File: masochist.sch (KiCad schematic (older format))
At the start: 76 parts, among them Y1 Crystal

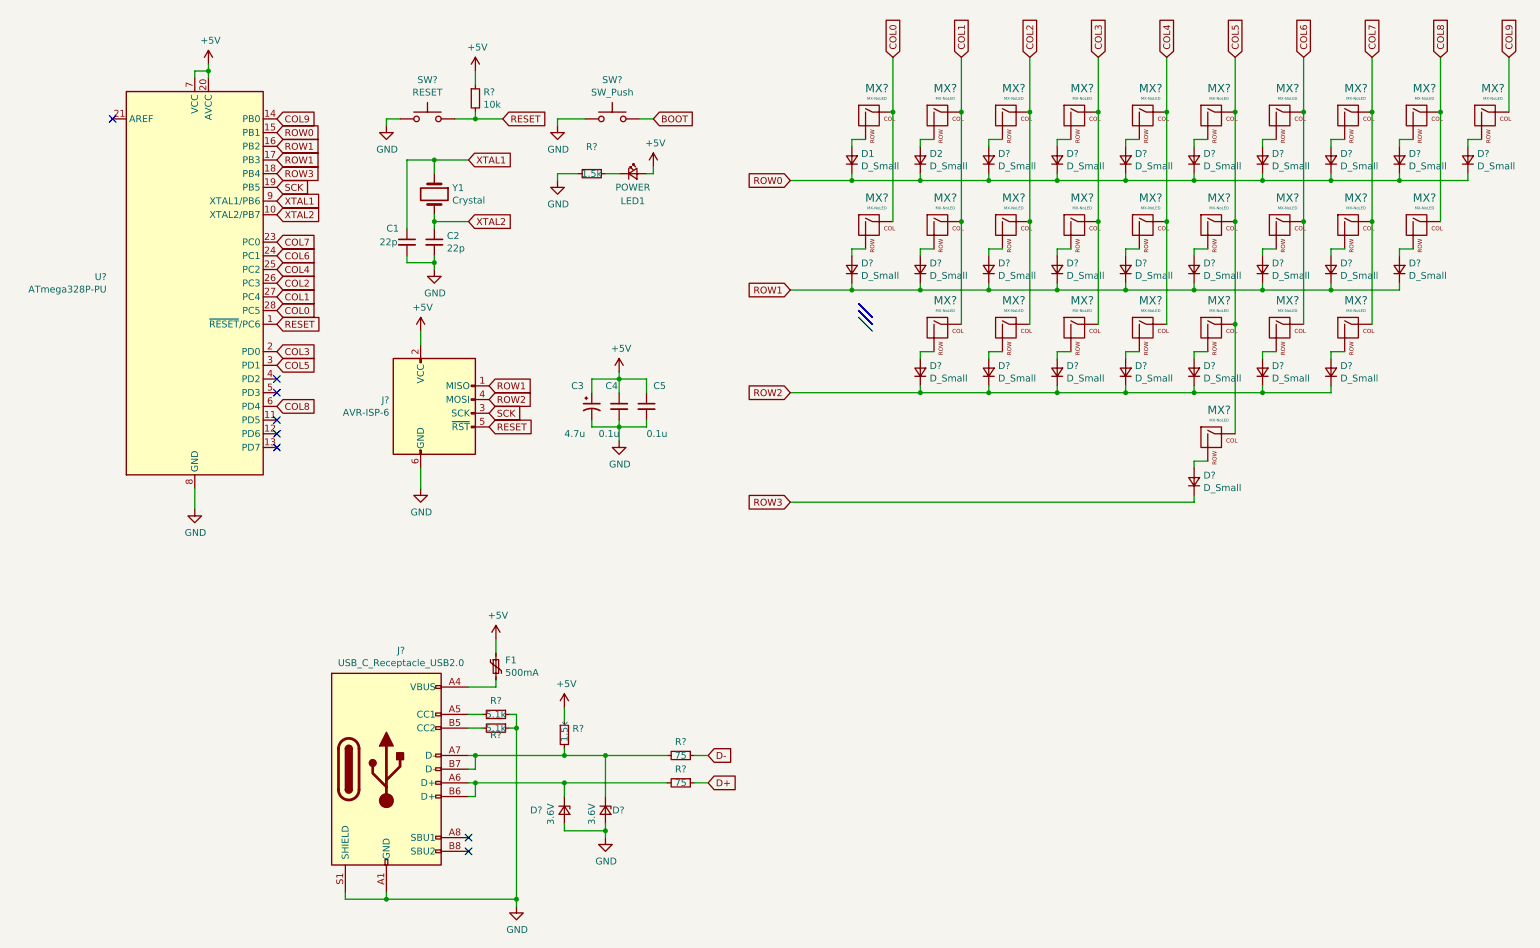
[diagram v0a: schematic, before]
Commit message: updated component names
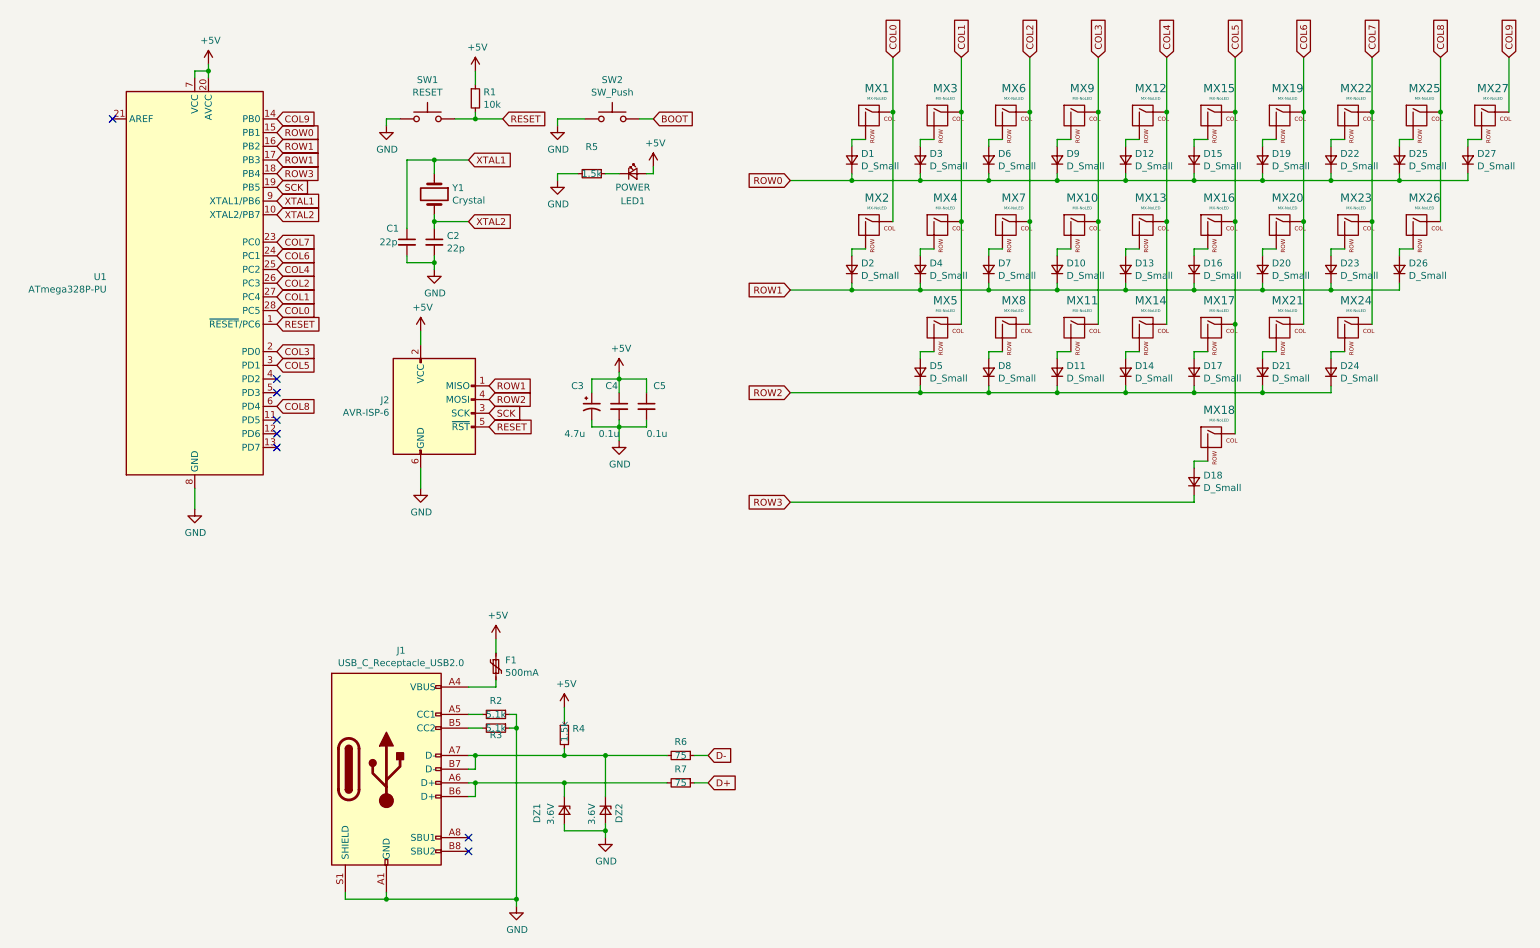
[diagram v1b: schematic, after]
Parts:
- gave numbers to parts that had none: 66
- renumbered D2 to D3

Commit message: started adding footprints
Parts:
- D1, D10, D11, D12, D13, D14, D15, D16, D17, D18, D19, D2, D20, D21, D22, D23, D24, D25, D26, D27, D3, D4, D5, D6, D7, D8, D9: footprint (none) -> cftkb:D_DO-35_SOD27_P5.08mm_Horizontal
- F1: footprint (none) -> cftkb:polyfuse_5.1mm
- J2: footprint (none) -> cftkb:AVR_ICSP_3x2
- LED1: footprint (none) -> cftkb:LED_D3.0mm
- SW1, SW2: footprint (none) -> cftkb:SW_PUSH_6mm
- Y1: footprint (none) -> cftkb:Crystal_HC49-4H_Vertical
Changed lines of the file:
@@
 F 0 "D1" V 6346 1432 50  0000 R CNN
 F 1 "D_Small" V 6255 1432 50  0000 R CNN
-F 2 "" V 6300 1500 50  0001 C CNN
+F 2 "cftkb:D_DO-35_SOD27_P5.08mm_Horizontal" V 6300 1500 50  0001 C CNN
 F 3 "~" V 6300 1500 50  0001 C CNN
 	1    6300 1500
@@
 F 0 "D3" V 6846 1432 50  0000 R CNN
 F 1 "D_Small" V 6755 1432 50  0000 R CNN
-F 2 "" V 6800 1500 50  0001 C CNN
+F 2 "cftkb:D_DO-35_SOD27_P5.08mm_Horizontal" V 6800 1500 50  0001 C CNN
 F 3 "~" V 6800 1500 50  0001 C CNN
 	1    6800 1500
@@
 F 0 "D6" V 7346 1432 50  0000 R CNN
 F 1 "D_Small" V 7255 1432 50  0000 R CNN
-F 2 "" V 7300 1500 50  0001 C CNN
+F 2 "cftkb:D_DO-35_SOD27_P5.08mm_Horizontal" V 7300 1500 50  0001 C CNN
 F 3 "~" V 7300 1500 50  0001 C CNN
 	1    7300 1500
@@
 F 0 "D9" V 7846 1432 50  0000 R CNN
 F 1 "D_Small" V 7755 1432 50  0000 R CNN
-F 2 "" V 7800 1500 50  0001 C CNN
+F 2 "cftkb:D_DO-35_SOD27_P5.08mm_Horizontal" V 7800 1500 50  0001 C CNN
 F 3 "~" V 7800 1500 50  0001 C CNN
 	1    7800 1500
@@
 F 0 "D12" V 8346 1432 50  0000 R CNN
 F 1 "D_Small" V 8255 1432 50  0000 R CNN
-F 2 "" V 8300 1500 50  0001 C CNN
+F 2 "cftkb:D_DO-35_SOD27_P5.08mm_Horizontal" V 8300 1500 50  0001 C CNN
 F 3 "~" V 8300 1500 50  0001 C CNN
 	1    8300 1500
@@
 F 0 "D15" V 8846 1432 50  0000 R CNN
 F 1 "D_Small" V 8755 1432 50  0000 R CNN
-F 2 "" V 8800 1500 50  0001 C CNN
+F 2 "cftkb:D_DO-35_SOD27_P5.08mm_Horizontal" V 8800 1500 50  0001 C CNN
 F 3 "~" V 8800 1500 50  0001 C CNN
 	1    8800 1500
@@
 F 0 "D19" V 9346 1432 50  0000 R CNN
 F 1 "D_Small" V 9255 1432 50  0000 R CNN
-F 2 "" V 9300 1500 50  0001 C CNN
+F 2 "cftkb:D_DO-35_SOD27_P5.08mm_Horizontal" V 9300 1500 50  0001 C CNN
 F 3 "~" V 9300 1500 50  0001 C CNN
 	1    9300 1500
@@
 F 0 "D22" V 9846 1432 50  0000 R CNN
 F 1 "D_Small" V 9755 1432 50  0000 R CNN
-F 2 "" V 9800 1500 50  0001 C CNN
+F 2 "cftkb:D_DO-35_SOD27_P5.08mm_Horizontal" V 9800 1500 50  0001 C CNN
 F 3 "~" V 9800 1500 50  0001 C CNN
 	1    9800 1500
@@
 F 0 "D25" V 10346 1432 50  0000 R CNN
 F 1 "D_Small" V 10255 1432 50  0000 R CNN
-F 2 "" V 10300 1500 50  0001 C CNN
+F 2 "cftkb:D_DO-35_SOD27_P5.08mm_Horizontal" V 10300 1500 50  0001 C CNN
 F 3 "~" V 10300 1500 50  0001 C CNN
 	1    10300 1500
@@
 F 0 "D27" V 10846 1432 50  0000 R CNN
 F 1 "D_Small" V 10755 1432 50  0000 R CNN
-F 2 "" V 10800 1500 50  0001 C CNN
+F 2 "cftkb:D_DO-35_SOD27_P5.08mm_Horizontal" V 10800 1500 50  0001 C CNN
 F 3 "~" V 10800 1500 50  0001 C CNN
 	1    10800 1500
@@
 F 0 "D2" V 6346 2232 50  0000 R CNN
 F 1 "D_Small" V 6255 2232 50  0000 R CNN
-F 2 "" V 6300 2300 50  0001 C CNN
+F 2 "cftkb:D_DO-35_SOD27_P5.08mm_Horizontal" V 6300 2300 50  0001 C CNN
 F 3 "~" V 6300 2300 50  0001 C CNN
 	1    6300 2300
@@
 F 0 "D4" V 6846 2232 50  0000 R CNN
 F 1 "D_Small" V 6755 2232 50  0000 R CNN
-F 2 "" V 6800 2300 50  0001 C CNN
+F 2 "cftkb:D_DO-35_SOD27_P5.08mm_Horizontal" V 6800 2300 50  0001 C CNN
 F 3 "~" V 6800 2300 50  0001 C CNN
 	1    6800 2300
@@
 F 0 "D7" V 7346 2232 50  0000 R CNN
 F 1 "D_Small" V 7255 2232 50  0000 R CNN
-F 2 "" V 7300 2300 50  0001 C CNN
+F 2 "cftkb:D_DO-35_SOD27_P5.08mm_Horizontal" V 7300 2300 50  0001 C CNN
 F 3 "~" V 7300 2300 50  0001 C CNN
 	1    7300 2300
@@
 F 0 "D10" V 7846 2232 50  0000 R CNN
 F 1 "D_Small" V 7755 2232 50  0000 R CNN
-F 2 "" V 7800 2300 50  0001 C CNN
+F 2 "cftkb:D_DO-35_SOD27_P5.08mm_Horizontal" V 7800 2300 50  0001 C CNN
 F 3 "~" V 7800 2300 50  0001 C CNN
 	1    7800 2300
@@
 F 0 "D13" V 8346 2232 50  0000 R CNN
 F 1 "D_Small" V 8255 2232 50  0000 R CNN
-F 2 "" V 8300 2300 50  0001 C CNN
+F 2 "cftkb:D_DO-35_SOD27_P5.08mm_Horizontal" V 8300 2300 50  0001 C CNN
 F 3 "~" V 8300 2300 50  0001 C CNN
 	1    8300 2300
@@
 F 0 "D16" V 8846 2232 50  0000 R CNN
 F 1 "D_Small" V 8755 2232 50  0000 R CNN
-F 2 "" V 8800 2300 50  0001 C CNN
+F 2 "cftkb:D_DO-35_SOD27_P5.08mm_Horizontal" V 8800 2300 50  0001 C CNN
 F 3 "~" V 8800 2300 50  0001 C CNN
 	1    8800 2300
@@
 F 0 "D20" V 9346 2232 50  0000 R CNN
 F 1 "D_Small" V 9255 2232 50  0000 R CNN
-F 2 "" V 9300 2300 50  0001 C CNN
+F 2 "cftkb:D_DO-35_SOD27_P5.08mm_Horizontal" V 9300 2300 50  0001 C CNN
 F 3 "~" V 9300 2300 50  0001 C CNN
 	1    9300 2300
@@
 F 0 "D23" V 9846 2232 50  0000 R CNN
 F 1 "D_Small" V 9755 2232 50  0000 R CNN
-F 2 "" V 9800 2300 50  0001 C CNN
+F 2 "cftkb:D_DO-35_SOD27_P5.08mm_Horizontal" V 9800 2300 50  0001 C CNN
 F 3 "~" V 9800 2300 50  0001 C CNN
 	1    9800 2300
@@
 F 0 "D26" V 10346 2232 50  0000 R CNN
 F 1 "D_Small" V 10255 2232 50  0000 R CNN
-F 2 "" V 10300 2300 50  0001 C CNN
+F 2 "cftkb:D_DO-35_SOD27_P5.08mm_Horizontal" V 10300 2300 50  0001 C CNN
 F 3 "~" V 10300 2300 50  0001 C CNN
 	1    10300 2300
@@
 F 0 "D5" V 6846 2982 50  0000 R CNN
 F 1 "D_Small" V 6755 2982 50  0000 R CNN
-F 2 "" V 6800 3050 50  0001 C CNN
+F 2 "cftkb:D_DO-35_SOD27_P5.08mm_Horizontal" V 6800 3050 50  0001 C CNN
 F 3 "~" V 6800 3050 50  0001 C CNN
 	1    6800 3050
@@
 F 0 "D8" V 7346 2982 50  0000 R CNN
 F 1 "D_Small" V 7255 2982 50  0000 R CNN
-F 2 "" V 7300 3050 50  0001 C CNN
+F 2 "cftkb:D_DO-35_SOD27_P5.08mm_Horizontal" V 7300 3050 50  0001 C CNN
 F 3 "~" V 7300 3050 50  0001 C CNN
 	1    7300 3050
@@
 F 0 "D11" V 7846 2982 50  0000 R CNN
 F 1 "D_Small" V 7755 2982 50  0000 R CNN
-F 2 "" V 7800 3050 50  0001 C CNN
+F 2 "cftkb:D_DO-35_SOD27_P5.08mm_Horizontal" V 7800 3050 50  0001 C CNN
 F 3 "~" V 7800 3050 50  0001 C CNN
 	1    7800 3050
@@
 F 0 "D14" V 8346 2982 50  0000 R CNN
 F 1 "D_Small" V 8255 2982 50  0000 R CNN
-F 2 "" V 8300 3050 50  0001 C CNN
+F 2 "cftkb:D_DO-35_SOD27_P5.08mm_Horizontal" V 8300 3050 50  0001 C CNN
 F 3 "~" V 8300 3050 50  0001 C CNN
 	1    8300 3050
@@
 F 0 "D17" V 8846 2982 50  0000 R CNN
 F 1 "D_Small" V 8755 2982 50  0000 R CNN
-F 2 "" V 8800 3050 50  0001 C CNN
+F 2 "cftkb:D_DO-35_SOD27_P5.08mm_Horizontal" V 8800 3050 50  0001 C CNN
 F 3 "~" V 8800 3050 50  0001 C CNN
 	1    8800 3050
@@
 F 0 "D21" V 9346 2982 50  0000 R CNN
 F 1 "D_Small" V 9255 2982 50  0000 R CNN
-F 2 "" V 9300 3050 50  0001 C CNN
+F 2 "cftkb:D_DO-35_SOD27_P5.08mm_Horizontal" V 9300 3050 50  0001 C CNN
 F 3 "~" V 9300 3050 50  0001 C CNN
 	1    9300 3050
@@
 F 0 "D24" V 9846 2982 50  0000 R CNN
 F 1 "D_Small" V 9755 2982 50  0000 R CNN
-F 2 "" V 9800 3050 50  0001 C CNN
+F 2 "cftkb:D_DO-35_SOD27_P5.08mm_Horizontal" V 9800 3050 50  0001 C CNN
 F 3 "~" V 9800 3050 50  0001 C CNN
 	1    9800 3050
@@
 F 0 "D18" V 8846 3782 50  0000 R CNN
 F 1 "D_Small" V 8755 3782 50  0000 R CNN
-F 2 "" V 8800 3850 50  0001 C CNN
+F 2 "cftkb:D_DO-35_SOD27_P5.08mm_Horizontal" V 8800 3850 50  0001 C CNN
 F 3 "~" V 8800 3850 50  0001 C CNN
 	1    8800 3850
@@
 F 0 "Y1" V 3204 1881 50  0000 L CNN
 F 1 "Crystal" V 3295 1881 50  0000 L CNN
-F 2 "" H 3250 1750 50  0001 C CNN
+F 2 "cftkb:Crystal_HC49-4H_Vertical" H 3250 1750 50  0001 C CNN
 F 3 "~" H 3250 1750 50  0001 C CNN
 	1    3250 1750
@@
 F 0 "J2" H 2921 3446 50  0000 R CNN
 F 1 "AVR-ISP-6" H 2921 3355 50  0000 R CNN
-F 2 "" V 3000 3400 50  0001 C CNN
+F 2 "cftkb:AVR_ICSP_3x2" V 3000 3400 50  0001 C CNN
 F 3 " ~" H 1975 2800 50  0001 C CNN
 	1    3250 3350
@@
 F 0 "SW1" H 3200 1485 50  0000 C CNN
 F 1 "RESET" H 3200 1394 50  0000 C CNN
-F 2 "" H 3200 1400 50  0001 C CNN
+F 2 "cftkb:SW_PUSH_6mm" H 3200 1400 50  0001 C CNN
 F 3 "~" H 3200 1400 50  0001 C CNN
 	1    3200 1200
@@
 F 0 "F1" H 3768 5246 50  0000 L CNN
 F 1 "500mA" H 3768 5155 50  0000 L CNN
-F 2 "" H 3750 5000 50  0001 L CNN
+F 2 "cftkb:polyfuse_5.1mm" H 3750 5000 50  0001 L CNN
 F 3 "~" H 3700 5200 50  0001 C CNN
 	1    3700 5200
@@
 F 0 "SW2" H 4550 1485 50  0000 C CNN
 F 1 "SW_Push" H 4550 1394 50  0000 C CNN
-F 2 "" H 4550 1400 50  0001 C CNN
+F 2 "cftkb:SW_PUSH_6mm" H 4550 1400 50  0001 C CNN
 F 3 "~" H 4550 1400 50  0001 C CNN
 	1    4550 1200
@@
 F 0 "LED1" H 4700 1400 50  0000 C CNN
 F 1 "POWER" H 4700 1500 50  0000 C CNN
-F 2 "" V 4700 1600 50  0001 C CNN
+F 2 "cftkb:LED_D3.0mm" V 4700 1600 50  0001 C CNN
 F 3 "~" V 4700 1600 50  0001 C CNN
 	1    4700 1600

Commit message: spaghetti mess of a pcb
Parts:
- C1, C2: footprint (none) -> cftkb:C_Disc_D3.0mm_W1.6mm_P2.50mm
- C3: footprint (none) -> cftkb:CP_Radial_D4.0mm_P1.50mm
- C4, C5: footprint (none) -> cftkb:C_Disc_D4.3mm_W1.9mm_P5.00mm
- DZ1, DZ2: footprint (none) -> cftkb:D_DO-35_SOD27_P5.08mm_Horizontal
- J1: footprint (none) -> cftkb:USB_C_GCT_USB4085
- MX1, MX10, MX11, MX12, MX13, MX14, MX15, MX16, MX17, MX18, MX19, MX2, MX20, MX21, MX22, MX23, MX24, MX25, MX26, MX27, MX3, MX4, MX5, MX6, MX7, MX8, MX9: footprint (none) -> cftkb:SW_Cherry_MX1A_1.00u_PCB-NOSCREEN
- R1, R2, R3, R4, R5, R6, R7: footprint (none) -> cftkb:R_Axial_DIN0204_L3.6mm_D1.6mm_P5.08mm_Horizontal
